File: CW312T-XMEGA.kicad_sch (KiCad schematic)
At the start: 7 parts, among them P1 PCIEx4 EDGE CONNECTOR, U1 ATXMEGA128D4-AU

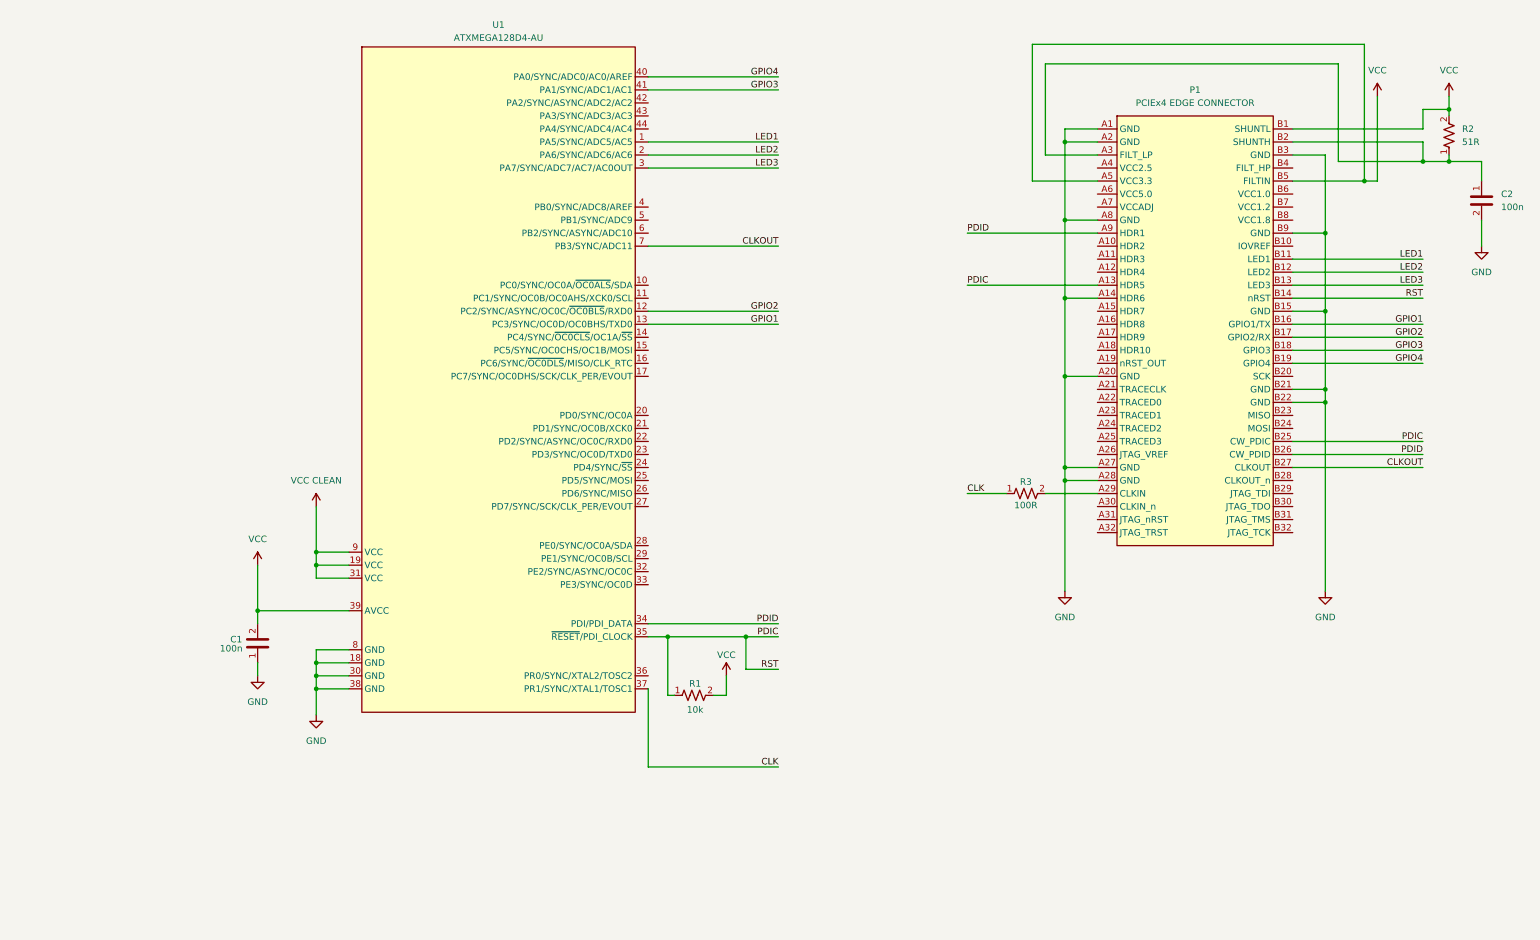
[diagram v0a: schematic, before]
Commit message: Draft of CW312T-XMEGA target - ready for review
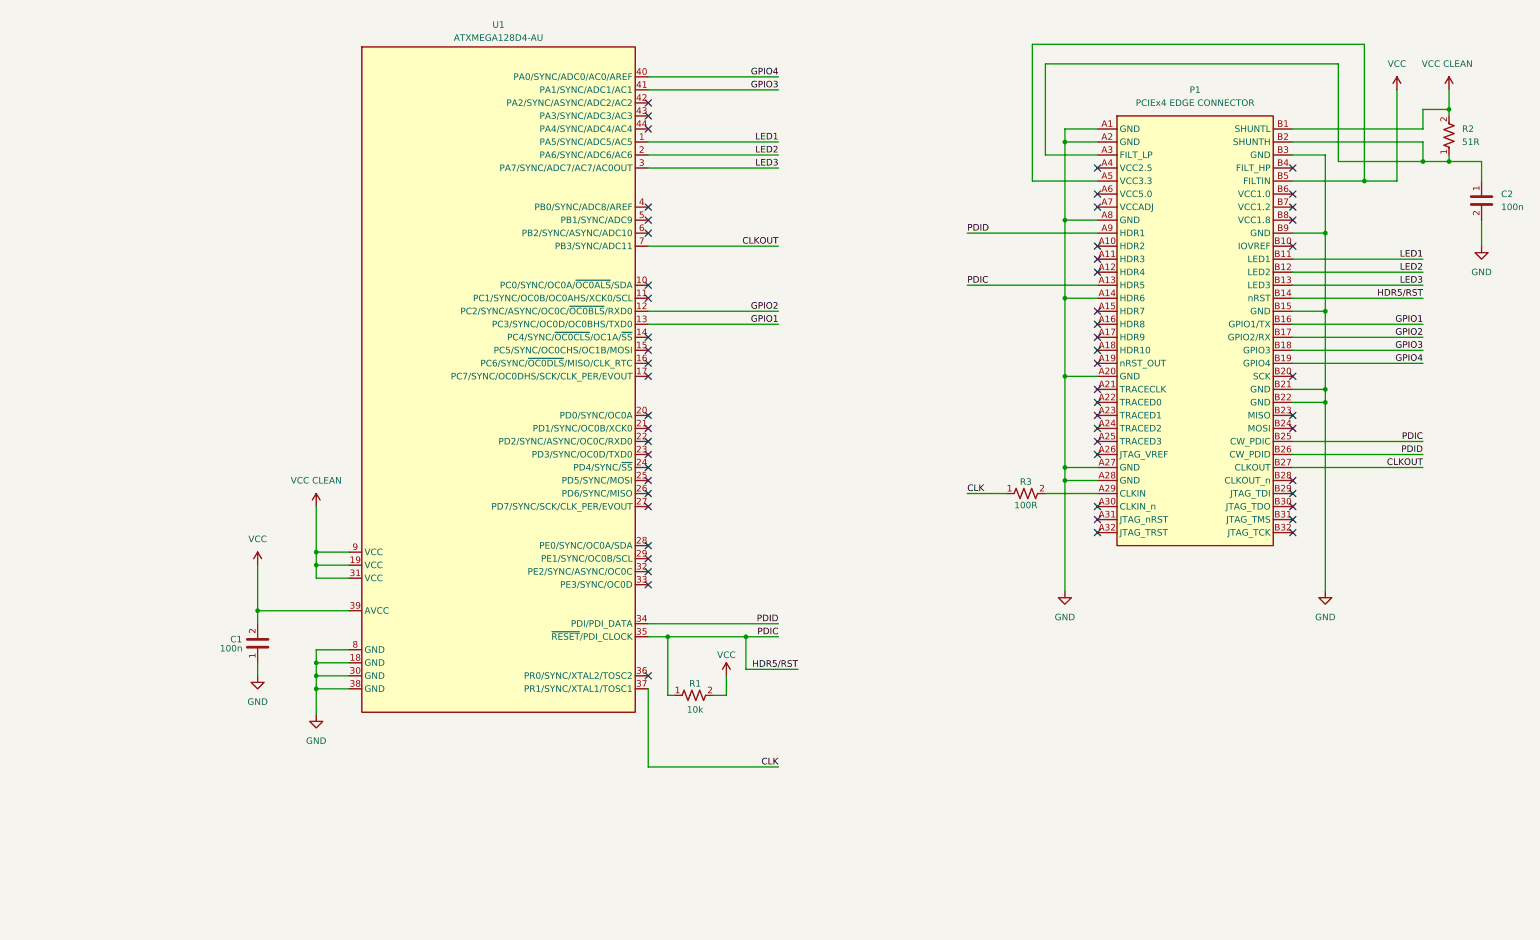
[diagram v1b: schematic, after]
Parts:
- added PCB1: CE, Silkscrren_Symbols:CE-Logo_8.5x6mm_SilkScreen, symbol Silkscreen_Symbols:CE_Free
- added PCB2: Pb_Free, Silkscrren_Symbols:Pb_Free_8.0x8.0mm_SilkScreen, symbol Silkscreen_Symbols:Pb_Free
- added PCB3: WEEE, Silkscrren_Symbols:WEEE-Logo_5.6x8mm_SilkScreen, symbol Silkscreen_Symbols:WEEE
- U1: footprint Package_QFP:TQFP-64-1EP_10x10mm_P0.5mm_EP8x8mm -> Package_QFP:TQFP-44_10x10mm_P0.8mm
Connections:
- net VCC: no longer P1.B1 (SHUNTL), R2.2
- net VCC CLEAN: now also P1.B1 (SHUNTL), R2.2
- net PDIC renamed HDR5/RST
- no-connect marks 0 -> 58

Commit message: updated silkscreen and schematic
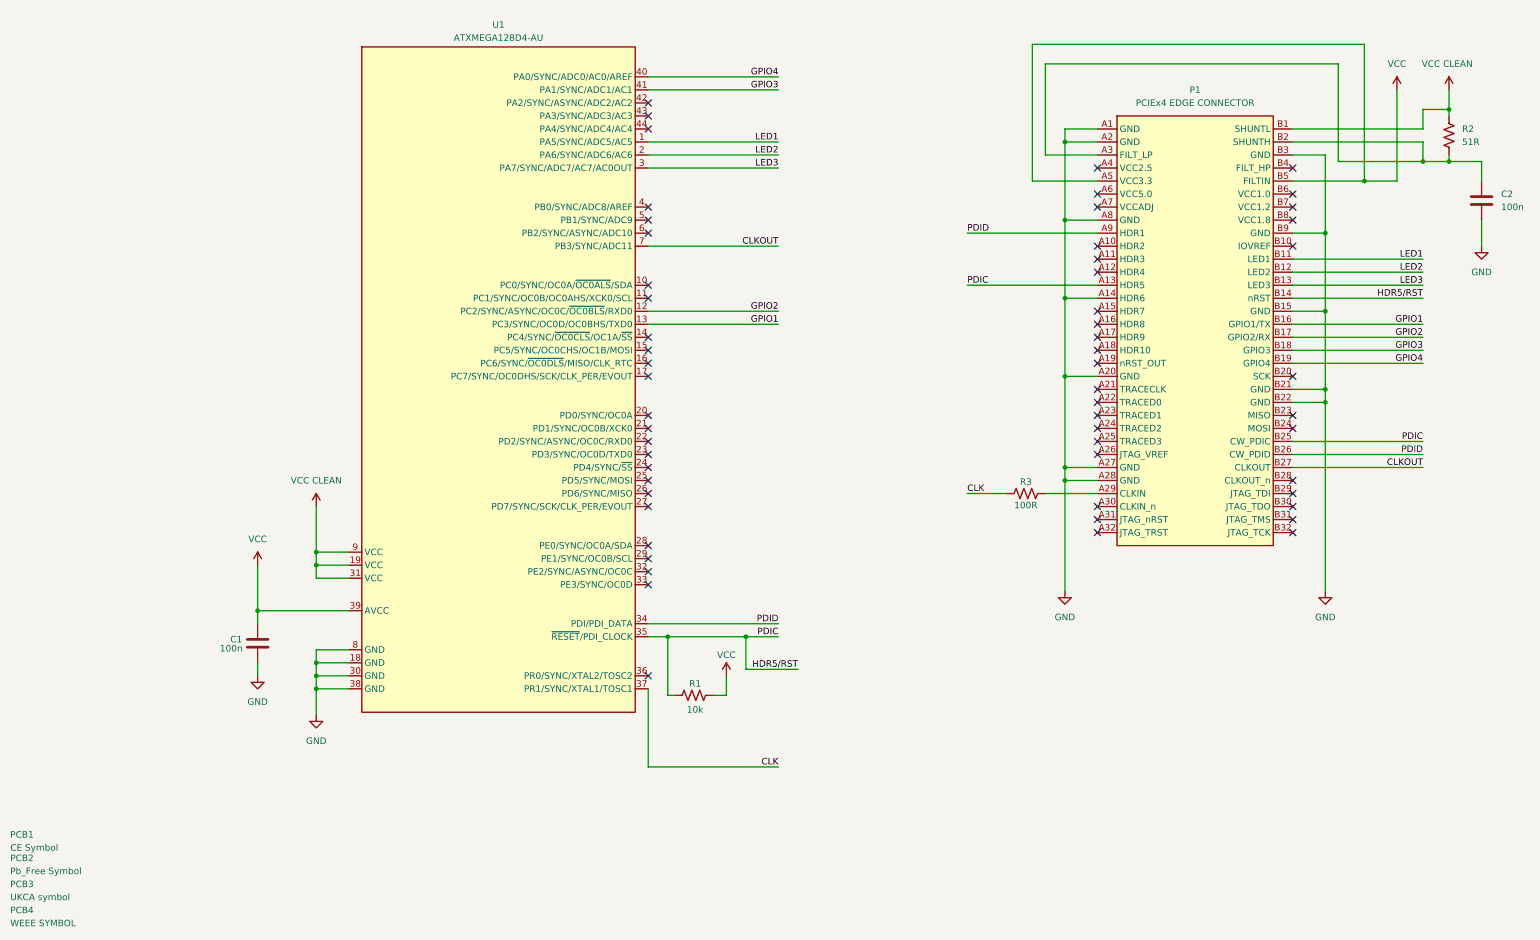
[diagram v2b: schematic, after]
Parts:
- removed PCB3: WEEE, Silkscrren_Symbols:WEEE-Logo_5.6x8mm_SilkScreen, symbol Silkscreen_Symbols:WEEE
- added PCB3: UKCA symbol, Silkscrren_Symbols:UKCA-Logo_8x8mm_SilkScreen, symbol Silkscreen_Symbols:UKCA
- added PCB4: WEEE SYMBOL, Silkscrren_Symbols:WEEE-Logo_5.6x8mm_SilkScreen, symbol Silkscreen_Symbols:WEEE
- PCB1: value CE -> CE Symbol
- PCB2: value Pb_Free -> Pb_Free Symbol
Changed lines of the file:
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@@
-	)
-	(symbol
-		(lib_id "Silkscreen_Symbols:CE_Free")
-		(at 21.59 180.34 0)
-		(unit 1)
-		(exclude_from_sim no)
-		(in_bom no)
-		(on_board yes)
-		(dnp no)
-		(fields_autoplaced yes)
-		(property "Reference" "PCB1"
-			(at 19.05 173.99 0)
-			(effects
-				(font
-					(size 1.27 1.27)
-				)
-				(hide yes)
-			)
-		)
-		(property "Value" "CE"
-			(at 21.59 180.34 0)
-			(effects
-				(font
-					(size 1.27 1.27)
-				)
-				(hide yes)
-			)
-		)
-		(property "Footprint" "Silkscrren_Symbols:CE-Logo_8.5x6mm_SilkScreen"
-			(at 21.59 180.34 0)
-			(effects
-				(font
-					(size 1.27 1.27)
-				)
-				(hide yes)
-			)
-		)
-		(property "Datasheet" ""
-			(at 21.59 180.34 0)
-			(effects
-				(font
-					(size 1.27 1.27)
-				)
-				(hide yes)
-			)
-		)
-		(property "Description" ""
-			(at 21.59 180.34 0)
-			(effects
-				(font
-					(size 1.27 1.27)
-				)
-				(hide yes)
-			)
-		)
-		(instances
-			(project ""
-				(path "/3926612a-0500-4374-ab4a-d31e50fcc6a5"
-					(reference "PCB1")
-					(unit 1)
-				)
-			)
-		)
 	)
 	(symbol
@@
 	)
 	(symbol
+		(lib_id "Silkscreen_Symbols:UKCA")
+		(at -22.86 194.31 0)
+		(unit 1)
+		(exclude_from_sim no)
+		(in_bom yes)
+		(on_board yes)
+		(dnp no)
+		(fields_autoplaced yes)
+		(property "Reference" "PCB3"
+			(at -20.32 193.0399 0)
+			(effects
+				(font
+					(size 1.27 1.27)
+				)
+				(justify left)
+			)
+		)
+		(property "Value" "UKCA symbol"
+			(at -20.32 195.5799 0)
+			(effects
+				(font
+					(size 1.27 1.27)
+				)
+				(justify left)
+			)
+		)
+		(property "Footprint" "Silkscrren_Symbols:UKCA-Logo_8x8mm_SilkScreen"
+			(at -22.86 194.31 0)
+			(effects
+				(font
+					(size 1.27 1.27)
+				)
+				(hide yes)
+			)
+		)
+		(property "Datasheet" ""
+			(at -22.86 194.31 0)
+			(effects
+				(font
+					(size 1.27 1.27)
+				)
+				(hide yes)
+			)
+		)
+		(property "Description" ""
+			(at -22.86 194.31 0)
+			(effects
+				(font
+					(size 1.27 1.27)
+				)
+				(hide yes)
+			)
+		)
+		(instances
+			(project ""
+				(path "/3926612a-0500-4374-ab4a-d31e50fcc6a5"
+					(reference "PCB3")
+					(unit 1)
+				)
+			)
+		)
+	)
+	(symbol
 		(lib_id "nae_caps:CAP_100n_6.3V_0603")
 		(at 266.7 59.69 270)
@@
 	)
 	(symbol
+		(lib_id "Silkscreen_Symbols:CE_Free")
+		(at -31.75 176.53 0)
+		(unit 1)
+		(exclude_from_sim no)
+		(in_bom no)
+		(on_board yes)
+		(dnp no)
+		(property "Reference" "PCB1"
+			(at -20.32 183.388 0)
+			(effects
+				(font
+					(size 1.27 1.27)
+				)
+				(justify left)
+			)
+		)
+		(property "Value" "CE Symbol"
+			(at -20.32 185.928 0)
+			(effects
+				(font
+					(size 1.27 1.27)
+				)
+				(justify left)
+			)
+		)
+		(property "Footprint" "Silkscrren_Symbols:CE-Logo_8.5x6mm_SilkScreen"
+			(at -31.75 176.53 0)
+			(effects
+				(font
+					(size 1.27 1.27)
+				)
+				(hide yes)
+			)
+		)
+		(property "Datasheet" ""
+			(at -31.75 176.53 0)
+			(effects
+				(font
+					(size 1.27 1.27)
+				)
+				(hide yes)
+			)
+		)
+		(property "Description" ""
+			(at -31.75 176.53 0)
+			(effects
+				(font
+					(size 1.27 1.27)
+				)
+				(hide yes)
+			)
+		)
+		(instances
+			(project ""
+				(path "/3926612a-0500-4374-ab4a-d31e50fcc6a5"
+					(reference "PCB1")
+					(unit 1)
+				)
+			)
+		)
+	)
+	(symbol
 		(lib_id "tutorial_2_library:CW312T-Template")
 		(at 210.82 45.72 0)
@@
 	)
 	(symbol
+		(lib_id "Silkscreen_Symbols:WEEE")
+		(at -21.59 199.39 0)
+		(unit 1)
+		(exclude_from_sim no)
+		(in_bom no)
+		(on_board yes)
+		(dnp no)
+		(property "Reference" "PCB4"
+			(at -20.32 198.12 0)
+			(effects
+				(font
+					(size 1.27 1.27)
+				)
+				(justify left)
+			)
+		)
+		(property "Value" "WEEE SYMBOL"
+			(at -20.32 200.66 0)
+			(effects
+				(font
+					(size 1.27 1.27)
+				)
+				(justify left)
+			)
+		)
+		(property "Footprint" "Silkscrren_Symbols:WEEE-Logo_5.6x8mm_SilkScreen"
+			(at -21.59 199.39 0)
+			(effects
+				(font
+					(size 1.27 1.27)
+				)
+				(hide yes)
+			)
+		)
+		(property "Datasheet" ""
+			(at -21.59 199.39 0)
+			(effects
+				(font
+					(size 1.27 1.27)
+				)
+				(hide yes)
+			)
+		)
+		(property "Description" ""
+			(at -21.59 199.39 0)
+			(effects
+				(font
+					(size 1.27 1.27)
+				)
+				(hide yes)
+			)
+		)
+		(instances
+			(project ""
+				(path "/3926612a-0500-4374-ab4a-d31e50fcc6a5"
+					(reference "PCB4")
+					(unit 1)
+				)
+			)
+		)
+	)
+	(symbol
 		(lib_id "power:VCC")
 		(at 27.94 130.81 0)
@@
 	)
 	(symbol
-		(lib_id "Silkscreen_Symbols:Pb_Free")
-		(at 19.05 182.88 0)
-		(unit 1)
-		(exclude_from_sim no)
-		(in_bom no)
-		(on_board yes)
-		(dnp no)
-		(fields_autoplaced yes)
-		(property "Reference" "PCB2"
-			(at 19.05 182.88 0)
-			(effects
-				(font
-					(size 1.27 1.27)
-				)
-				(hide yes)
-			)
-		)
-		(property "Value" "Pb_Free"
-			(at 19.05 182.88 0)
-			(effects
-				(font
-					(size 1.27 1.27)
-				)
-				(hide yes)
-			)
-		)
-		(property "Footprint" "Silkscrren_Symbols:Pb_Free_8.0x8.0mm_SilkScreen"
-			(at 19.05 182.88 0)
-			(effects
-				(font
-					(size 1.27 1.27)
-				)
-				(hide yes)
-			)
-		)
-		(property "Datasheet" ""
-			(at 19.05 182.88 0)
-			(effects
-				(font
-					(size 1.27 1.27)
-				)
-				(hide yes)
-			)
-		)
-		(property "Description" ""
-			(at 19.05 182.88 0)
-			(effects
-				(font
-					(size 1.27 1.27)
-				)
-				(hide yes)
-			)
-		)
-		(instances
-			(project ""
-				(path "/3926612a-0500-4374-ab4a-d31e50fcc6a5"
-					(reference "PCB2")
-					(unit 1)
-				)
-			)
-		)
-	)
-	(symbol
-		(lib_id "Silkscreen_Symbols:WEEE")
-		(at 19.05 194.31 0)
-		(unit 1)
-		(exclude_from_sim no)
-		(in_bom no)
-		(on_board yes)
-		(dnp no)
-		(fields_autoplaced yes)
-		(property "Reference" "PCB3"
-			(at 17.78 189.865 0)
-			(effects
-				(font
-					(size 1.27 1.27)
-				)
-				(hide yes)
-			)
-		)
-		(property "Value" "WEEE"
-			(at 19.05 194.31 0)
-			(effects
-				(font
-					(size 1.27 1.27)
-				)
-				(hide yes)
-			)
-		)
-		(property "Footprint" "Silkscrren_Symbols:WEEE-Logo_5.6x8mm_SilkScreen"
-			(at 19.05 194.31 0)
-			(effects
-				(font
-					(size 1.27 1.27)
-				)
-				(hide yes)
-			)
-		)
-		(property "Datasheet" ""
-			(at 19.05 194.31 0)
-			(effects
-				(font
-					(size 1.27 1.27)
-				)
-				(hide yes)
-			)
-		)
-		(property "Description" ""
-			(at 19.05 194.31 0)
-			(effects
-				(font
-					(size 1.27 1.27)
-				)
-				(hide yes)
-			)
-		)
-		(instances
-			(project ""
-				(path "/3926612a-0500-4374-ab4a-d31e50fcc6a5"
-					(reference "PCB3")
-					(unit 1)
-				)
-			)
-		)
-	)
-	(symbol
 		(lib_id "nae_caps:CAP_100n_6.3V_0603")
 		(at 27.94 146.05 90)
@@
 					(unit 1)
 				)
+			)
+		)
+	)
+	(symbol
+		(lib_id "Silkscreen_Symbols:Pb_Free")
+		(at -26.67 184.15 0)
+		(unit 1)
+		(exclude_from_sim no)
+		(in_bom no)
+		(on_board yes)
+		(dnp no)
+		(property "Reference" "PCB2"
+			(at -20.32 187.96 0)
+			(effects
+				(font
+					(size 1.27 1.27)
+				)
+				(justify left)
+			)
+		)
+		(property "Value" "Pb_Free Symbol"
+			(at -20.32 190.5 0)
+			(effects
+				(font
+					(size 1.27 1.27)
+				)
+				(justify left)
+			)
+		)
+		(property "Footprint" "Silkscrren_Symbols:Pb_Free_8.0x8.0mm_SilkScreen"
+			(at -26.67 184.15 0)
+			(effects
+				(font
+					(size 1.27 1.27)
+				)
+				(hide yes)
+			)
+		)
+		(property "Datasheet" ""
+			(at -26.67 184.15 0)
+			(effects
+				(font
+					(size 1.27 1.27)
+				)
+				(hide yes)
+			)
+		)
+		(property "Description" ""
+			(at -26.67 184.15 0)
+			(effects
+				(font
+					(size 1.27 1.27)
+				)
+				(hide yes)
+			)
+		)
+		(instances
+			(project ""
+				(path "/3926612a-0500-4374-ab4a-d31e50fcc6a5"
+					(reference "PCB2")
+					(unit 1)
+				)

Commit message: updated schematic and pcb - Ready for review
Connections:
- net FILT_LP: now reaches C2.1, P1.A3 (FILT_LP), P1.B2 (SHUNTH), R2.1
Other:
- moved on the sheet: C2, R1

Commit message: updated power on schematic and routing, updated silkscreen
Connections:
- net VCC: now also P1.A10 (HDR2), P1.B10 (IOVREF)
- no-connect marks 58 -> 56
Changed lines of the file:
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@@
+	)
+	(junction
+		(at 177.8 55.88)
+		(diameter 0)
+		(color 0 0 0 0)
 	)
 	(junction
@@
 	)
 	(junction
+		(at 243.84 55.88)
+		(diameter 0)
+		(color 0 0 0 0)
+	)
+	(junction
 		(at 39.37 154.94)
 		(diameter 0)
@@
 	)
 	(no_connect
-		(at 229.87 68.58)
-	)
-	(no_connect
 		(at 104.14 88.9)
 	)
@@
 	)
 	(no_connect
-		(at 191.77 68.58)
-	)
-	(no_connect
 		(at 104.14 66.04)
 	)
@@
 	(wire
 		(pts
+			(xy 191.77 68.58) (xy 177.8 68.58)
+		)
+		(stroke
+			(width 0)
+			(type default)
+		)
+	)
+	(wire
+		(pts
 			(xy 104.14 154.94) (xy 129.54 154.94)
 		)
@@
 	(wire
 		(pts
+			(xy 177.8 68.58) (xy 177.8 55.88)
+		)
+		(stroke
+			(width 0)
+			(type default)
+		)
+	)
+	(wire
+		(pts
 			(xy 111.76 138.43) (xy 111.76 144.78)
 		)
@@
 	(wire
 		(pts
+			(xy 229.87 68.58) (xy 243.84 68.58)
+		)
+		(stroke
+			(width 0)
+			(type default)
+		)
+	)
+	(wire
+		(pts
 			(xy 191.77 63.5) (xy 185.42 63.5)
 		)
@@
 		(pts
 			(xy 185.42 93.98) (xy 185.42 111.76)
+		)
+		(stroke
+			(width 0)
+			(type default)
+		)
+	)
+	(wire
+		(pts
+			(xy 243.84 68.58) (xy 243.84 55.88)
 		)
 		(stroke
@@
 		)
 	)
-	(label "FILTIN"
-		(at 177.8 55.88 0)
-		(fields_autoplaced yes)
-		(effects
-			(font
-				(size 1.27 1.27)
-			)
-			(justify left bottom)
-		)
-	)
 	(label "GPIO1"
 		(at 129.54 83.82 180)
@@
 		(fields_autoplaced yes)
 		(effects
-			(font
-				(size 1.27 1.27)
-			)
-			(justify right bottom)
-		)
-	)
-	(label "FILTIN"
-		(at 243.84 55.88 180)
-		(fields_autoplaced yes)
-		(effects

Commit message: updated schematic and pcb, after library reorganization
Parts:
- removed P1: PCIEx4 EDGE CONNECTOR, tutorial_2_library:CW312_Template, symbol tutorial_2_library:CW312T-Template
- removed U1: ATXMEGA128D4-AU, Package_QFP:TQFP-44_10x10mm_P0.8mm, symbol tutorial_2_library:ATXMEGA128D4-AU
- added P2: PCIEx4 EDGE CONNECTOR, tutorial_2_library:CW312_Template, symbol Connectors:CW312T-Template
- added U1: ATXMEGA128D4-AU, Package_QFP:TQFP-44_10x10mm_P0.8mm, symbol Integrated_Circuits:ATXMEGA128D4-AU
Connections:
- net CLK: now also U1.37 (PR1/SYNC/XTAL1/TOSC1)
- net CLKOUT: now also P2.B27 (CLKOUT), U1.7 (PB3/SYNC/ADC11)
- net FILT_LP: now also P2.A3 (FILT_LP), P2.B2 (SHUNTH)
- net GND: now also P2.A1 (GND), P2.A14 (HDR6), P2.A2 (GND), P2.A20 (GND), P2.A27 (GND), P2.A28 (GND), P2.A8 (GND), P2.B15 (GND), P2.B21 (GND), P2.B22 (GND), P2.B3 (GND), P2.B9 (GND), U1.18 (GND), U1.30 (GND), U1.38 (GND), U1.8 (GND)
- net GPIO1: now also P2.B16 (GPIO1/TX), U1.13 (PC3/SYNC/OC0D/OC0BHS/TXD0)
- net GPIO2: now also P2.B17 (GPIO2/RX), U1.12 (PC2/SYNC/ASYNC/OC0C/~{OC0BLS}/RXD0)
- net GPIO3: now also P2.B18 (GPIO3), U1.41 (PA1/SYNC/ADC1/AC1)
- net GPIO4: now also P2.B19 (GPIO4), U1.40 (PA0/SYNC/ADC0/AC0/AREF)
- net HDR5/RST: now also P2.A13 (HDR5), P2.B14 (nRST), P2.B25 (CW_PDIC), U1.35 (~{RESET}/PDI_CLOCK)
- net LED1: now also P2.B11 (LED1), U1.1 (PA5/SYNC/ADC5/AC5)
- net LED2: now also P2.B12 (LED2), U1.2 (PA6/SYNC/ADC6/AC6)
- net LED3: now also P2.B13 (LED3), U1.3 (PA7/SYNC/ADC7/AC7/AC0OUT)
- net PDID: now also P2.A9 (HDR1), P2.B26 (CW_PDID), U1.34 (PDI/PDI_DATA)
- net VCC: now also P2.A10 (HDR2), P2.A5 (VCC3.3), P2.B10 (IOVREF), P2.B5 (FILTIN), U1.39 (AVCC)
- net VCC CLEAN: now also P2.B1 (SHUNTL), U1.19 (VCC), U1.31 (VCC), U1.9 (VCC)
- net at R3.2: now also P2.A29 (CLKIN)
